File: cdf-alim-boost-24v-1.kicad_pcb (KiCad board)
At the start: 4 copper layers, 92 parts, among them J1 Conn_01x02, J2 Conn_01x02, J3 Conn_01x02, Q1 BSC019N04LS, Q2 BSC019N04LS, Q3 BSC019N04LS, Q4 BSC019N04LS, Q5 BSC019N04LS, U1 HT753-1, U2 TPS25983, U4 LM5122

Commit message: pcb: add +3V3 ldo layout
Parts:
- moved C1 7.19 mm to (191.5, 91.8), turned to 180 degrees
- moved TP4 6.05 mm to (196.5, 88.2), turned to 90 degrees
- moved C4 2.66 mm to (195.0, 91.8)
- moved U1 1.57 mm to (192.2, 87.8), turned to 90 degrees
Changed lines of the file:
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@@
 	(footprint "Capacitor_SMD:C_0805_2012Metric"
 		(layer "F.Cu")
-		(at 197.45 87.71)
+		(at 191.5 91.75 180)
 		(descr "Capacitor SMD 0805 (2012 Metric), square (rectangular) end terminal, IPC-7351 nominal, (Body size source: IPC-SM-782 page 76, https://www.pcb-3d.com/wordpress/wp-content/uploads/ipc-sm-782a_amendment_1_and_2.pdf, https://docs.google.com/spreadsheets/d/1BsfQQcO9C6DZCsRaXUlFlo91Tg2WpOkGARC1WS5S8t0/edit?usp=sharing)")
 		(tags "capacitor")
@@
 		)
 		(property "Basic" "Y"
-			(at 0 0 0)
+			(at 0 0 180)
 			(unlocked yes)
 			(layer "F.Fab")
@@
 		)
 		(property "JLCPCB Part #" "C440198"
-			(at 0 0 0)
+			(at 0 0 180)
 			(unlocked yes)
 			(layer "F.Fab")
@@
 		)
 		(property "Manufacturer" "Murata"
-			(at 0 0 0)
+			(at 0 0 180)
 			(unlocked yes)
 			(layer "F.Fab")
@@
 		)
 		(property "Manufacturer Part Number" "GRM21BR61H106KE43L"
-			(at 0 0 0)
+			(at 0 0 180)
 			(unlocked yes)
 			(layer "F.Fab")
@@
 		(duplicate_pad_numbers_are_jumpers no)
 		(fp_line
-			(start -0.261252 -0.735)
-			(end 0.261252 -0.735)
+			(start -0.261252 0.735)
+			(end 0.261252 0.735)
 			(stroke
 				(width 0.12)
@@
 		)
 		(fp_line
-			(start -0.261252 0.735)
-			(end 0.261252 0.735)
+			(start -0.261252 -0.735)
+			(end 0.261252 -0.735)
 			(stroke
 				(width 0.12)
@@
 		)
 		(pad "1" smd roundrect
-			(at -0.95 0)
+			(at -0.95 0 180)
 			(size 1 1.45)
 			(layers "F.Cu" "F.Mask" "F.Paste")
@@
 		)
 		(pad "2" smd roundrect
-			(at 0.95 0)
+			(at 0.95 0 180)
 			(size 1 1.45)
 			(layers "F.Cu" "F.Mask" "F.Paste")
@@
 	(footprint "TestPoint:TestPoint_Pad_D2.0mm"
 		(layer "F.Cu")
-		(at 197.25 94.25)
+		(at 196.5 88.25 90)
 		(descr "SMD pad as test Point, diameter 2.0mm")
 		(tags "test point SMD pad")
 		(property "Reference" "TP4"
-			(at 0 -1.998 0)
+			(at 0 -1.998 90)
 			(layer "F.SilkS")
 			(effects
@@
 		)
 		(property "Value" "TestPoint"
-			(at 0 2.05 0)
+			(at 0 2.05 90)
 			(layer "F.Fab")
 			(effects
@@
 		)
 		(property "Datasheet" ""
-			(at 0 0 0)
+			(at 0 0 90)
 			(unlocked yes)
 			(layer "F.Fab")
@@
 		)
 		(property "Description" "test point"
-			(at 0 0 0)
+			(at 0 0 90)
 			(unlocked yes)
 			(layer "F.Fab")
@@
 		)
 		(fp_text user "${REFERENCE}"
-			(at 0 -2 0)
+			(at 0 -2 90)
 			(layer "F.Fab")
 			(effects
@@
 		)
 		(pad "1" smd circle
-			(at 0 0)
+			(at 0 0 90)
 			(size 2 2)
 			(layers "F.Cu" "F.Mask")
@@
 	(footprint "Package_TO_SOT_SMD:SOT-89-3"
 		(layer "F.Cu")
-		(at 192.45 89.305)
+		(at 192.25 87.75 90)
 		(descr "SOT-89-3, http://ww1.microchip.com/downloads/en/DeviceDoc/3L_SOT-89_MB_C04-029C.pdf")
 		(tags "SOT-89-3")
 		(property "Reference" "U1"
-			(at 0 -3.5 0)
+			(at 0 -3.5 90)
 			(layer "F.SilkS")
 			(effects
@@
 		)
 		(property "Value" "HT753-1"
-			(at 0 3.5 0)
+			(at 0 3.5 90)
 			(layer "F.Fab")
 			(effects
@@
 		)
 		(property "Datasheet" "https://www.holtek.com/documents/10179/116711/HT75xx-1v250.pdf"
-			(at 0 0 0)
+			(at 0 0 90)
 			(unlocked yes)
 			(layer "F.Fab")
@@
 		)
 		(property "Description" "100mA Low Dropout Voltage Regulator, Fixed Output, SOT89"
-			(at 0 0 0)
+			(at 0 0 90)
 			(unlocked yes)
 			(layer "F.Fab")
@@
 		)
 		(property "Basic" "Y"
-			(at 0 0 0)
+			(at 0 0 90)
 			(unlocked yes)
 			(layer "F.Fab")
@@
 		)
 		(property "JLCPCB Part #" "C14289"
-			(at 0 0 0)
+			(at 0 0 90)
 			(unlocked yes)
 			(layer "F.Fab")
@@
 		)
 		(property "Manufacturer" "Holtek Semicon"
-			(at 0 0 0)
+			(at 0 0 90)
 			(unlocked yes)
 			(layer "F.Fab")
@@
 		)
 		(property "Manufacturer Part Number" "HT7533-1"
-			(at 0 0 0)
+			(at 0 0 90)
 			(unlocked yes)
 			(layer "F.Fab")
@@
 		)
 		(fp_line
-			(start -2.85 2.5)
+			(start 2.25 -2.5)
 			(end -2.85 -2.5)
 			(stroke
@@
 		)
 		(fp_line
-			(start -2.85 2.5)
+			(start 2.25 -2.5)
 			(end 2.25 2.5)
 			(stroke
@@
 		)
 		(fp_line
-			(start 2.25 -2.5)
+			(start -2.85 2.5)
 			(end -2.85 -2.5)
 			(stroke
@@
 		)
 		(fp_line
-			(start 2.25 -2.5)
+			(start -2.85 2.5)
 			(end 2.25 2.5)
 			(stroke
@@
 		)
 		(fp_line
-			(start -1.25 -1.25)
-			(end -0.25 -2.25)
+			(start 1.25 -2.25)
+			(end 1.25 2.25)
 			(stroke
 				(width 0.1)
@@
 		)
 		(fp_line
-			(start -1.25 2.25)
-			(end -1.25 -1.25)
+			(start -0.25 -2.25)
+			(end 1.25 -2.25)
 			(stroke
 				(width 0.1)
@@
 		)
 		(fp_line
-			(start -0.25 -2.25)
-			(end 1.25 -2.25)
+			(start -1.25 -1.25)
+			(end -0.25 -2.25)
 			(stroke
 				(width 0.1)
@@
 		)
 		(fp_line
-			(start 1.25 -2.25)
-			(end 1.25 2.25)
+			(start 1.25 2.25)
+			(end -1.25 2.25)
 			(stroke
 				(width 0.1)
@@
 		)
 		(fp_line
-			(start 1.25 2.25)
-			(end -1.25 2.25)
+			(start -1.25 2.25)
+			(end -1.25 -1.25)
 			(stroke
 				(width 0.1)
@@
 		)
 		(fp_text user "${REFERENCE}"
-			(at 0.2 0 90)
+			(at 0.2 0 0)
 			(layer "F.Fab")
 			(effects
@@
 		)
 		(pad "1" smd roundrect
-			(at -1.95 -1.5)
+			(at -1.95 -1.5 90)
 			(size 1.3 0.9)
 			(layers "F.Cu" "F.Mask" "F.Paste")
@@
 		)
 		(pad "2" smd custom
-			(at -1.8625 0)
+			(at -1.8625 0 90)
 			(size 1.475 0.9)
 			(layers "F.Cu" "F.Mask" "F.Paste")
@@
 		)
 		(pad "3" smd roundrect
-			(at -1.95 1.5)
+			(at -1.95 1.5 90)
 			(size 1.3 0.9)
 			(layers "F.Cu" "F.Mask" "F.Paste")
@@
 	(footprint "Capacitor_SMD:C_0805_2012Metric"
 		(layer "F.Cu")
-		(at 197.45 90.72)
+		(at 195 91.75)
 		(descr "Capacitor SMD 0805 (2012 Metric), square (rectangular) end terminal, IPC-7351 nominal, (Body size source: IPC-SM-782 page 76, https://www.pcb-3d.com/wordpress/wp-content/uploads/ipc-sm-782a_amendment_1_and_2.pdf, https://docs.google.com/spreadsheets/d/1BsfQQcO9C6DZCsRaXUlFlo91Tg2WpOkGARC1WS5S8t0/edit?usp=sharing)")
 		(tags "capacitor")

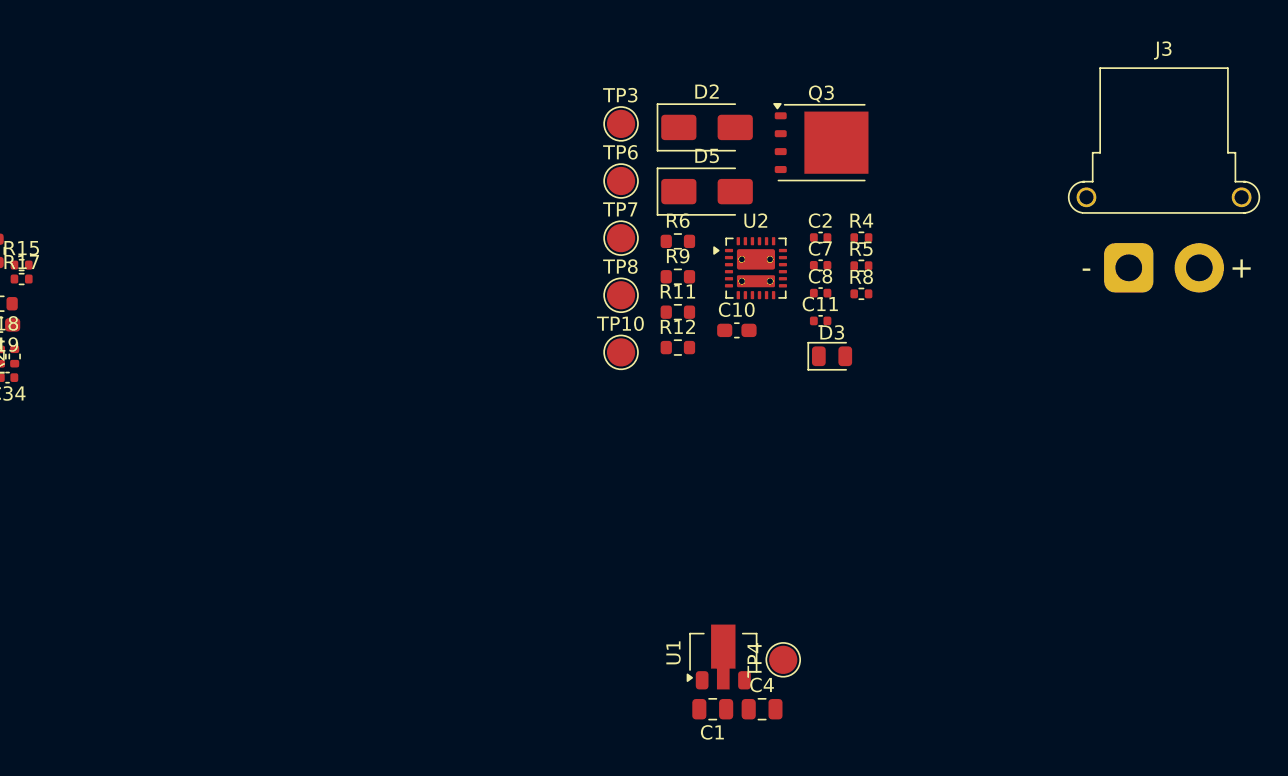
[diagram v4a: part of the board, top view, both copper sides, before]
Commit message: pcb: add efuse layout
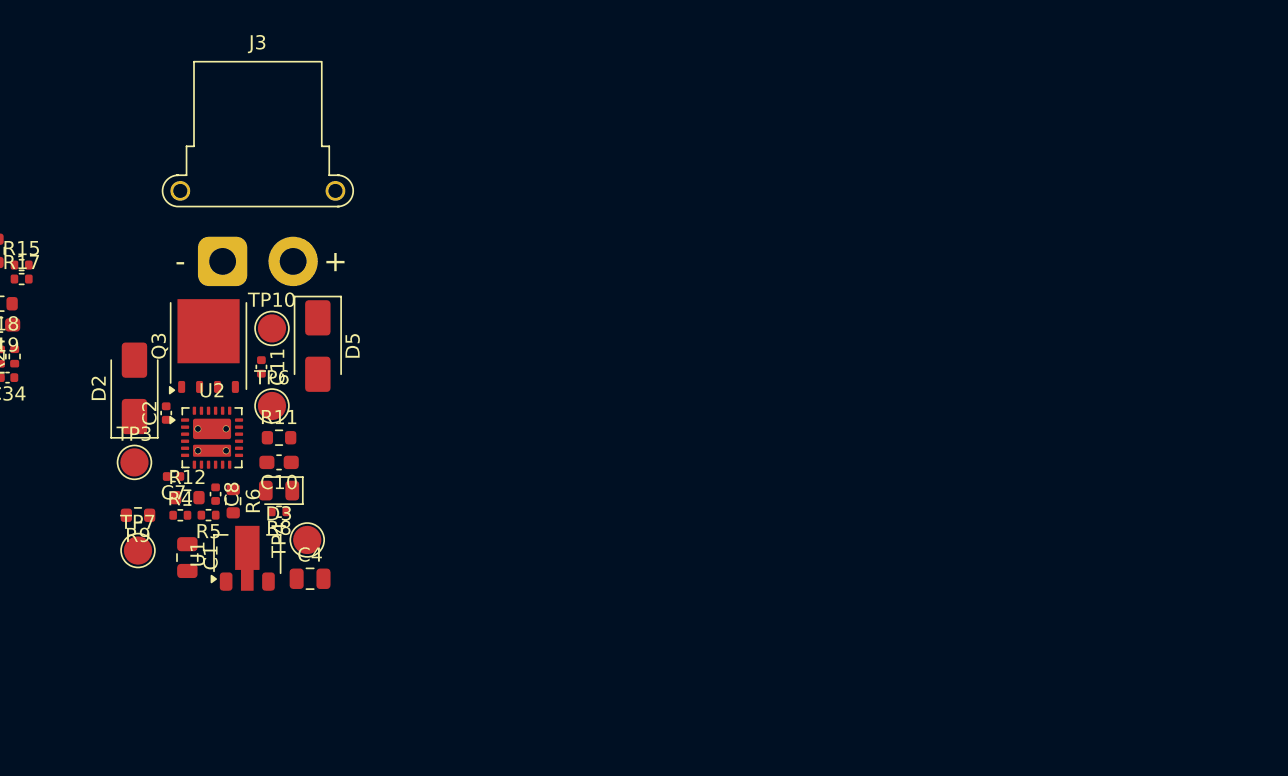
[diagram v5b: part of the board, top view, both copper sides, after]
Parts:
- removed TP8: TestPoint, TestPoint:TestPoint_Pad_D2.0mm
- moved J3 64.3 mm to (156.8, 60.0)
- moved R4 52.1 mm to (153.8, 78.0)
- moved R5 49.6 mm to (155.8, 78.0), turned to 180 degrees
- moved C7 48.3 mm to (153.3, 75.2), turned to 180 degrees
- moved C2 48.0 mm to (152.8, 70.8), turned to 90 degrees
- moved Q3 45.8 mm to (155.8, 66.0), turned to 90 degrees
- moved C8 45.2 mm to (156.2, 76.5), turned to -90 degrees
- moved D2 44.6 mm to (150.5, 69.0), turned to 90 degrees
- moved R8 44.1 mm to (160.8, 77.8), turned to 180 degrees
- moved TP3 42.0 mm to (150.5, 74.2)
- moved R9 41.8 mm to (150.8, 78.0), turned to 180 degrees
- moved TP7 40.8 mm to (150.8, 80.5)
- moved U2 40.4 mm to (156.0, 72.5)
- moved D3 40.4 mm to (160.8, 76.2), turned to 180 degrees
- moved C11 39.8 mm to (159.5, 67.5), turned to -90 degrees
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
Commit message: pcb: initial placement
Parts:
- removed TP11: TestPoint, TestPoint:TestPoint_Pad_D2.0mm
- added FID1: Fiducial, Fiducial:Fiducial_1mm_Mask2mm, F.Cu at (72.0, 81.0)
- added FID2: Fiducial, Fiducial:Fiducial_1mm_Mask2mm, F.Cu at (49.0, 58.0)
- added FID3: Fiducial, Fiducial:Fiducial_1mm_Mask2mm, F.Cu at (112.0, 61.0)
- added H1: MountingHole, MountingHole:ToolingHole_1.152mm, F.Cu at (60.0, 78.0)
- added H2: MountingHole, MountingHole:ToolingHole_1.152mm, F.Cu at (100.0, 83.0)
- added H3: MountingHole, MountingHole:ToolingHole_1.152mm, F.Cu at (78.0, 43.0)
- added H4: MountingHole_Pad, MountingHole:MountingHole_3.2mm_M3_Pad_Via, F.Cu at (66.0, 81.0)
- added H5: MountingHole_Pad, MountingHole:MountingHole_3.2mm_M3_Pad_Via, F.Cu at (88.0, 45.0)
- added H6: MountingHole_Pad, MountingHole:MountingHole_3.2mm_M3_Pad_Via, F.Cu at (111.0, 67.0)
- moved D5 99.4 mm to (66.0, 46.8), turned to 0 degrees
- moved J3 97.0 mm to (60.0, 53.5), turned to 90 degrees
- moved TP10 96.6 mm to (64.8, 50.0), turned to 90 degrees
- moved C11 93.5 mm to (67.5, 50.8), turned to 0 degrees
- moved TP6 92.2 mm to (70.2, 50.0), turned to 90 degrees
- moved R11 91.2 mm to (72.5, 49.5), turned to 90 degrees
- moved Q3 90.5 mm to (66.0, 54.5), turned to 180 degrees
- moved C10 90.0 mm to (74.2, 49.5), turned to -90 degrees
- moved TP4 89.0 mm to (79.8, 47.5), turned to 180 degrees
- moved D3 88.6 mm to (76.2, 49.5), turned to -90 degrees
- moved C4 87.8 mm to (82.5, 47.3), turned to 90 degrees
- moved R8 87.7 mm to (77.8, 49.5), turned to -90 degrees
- moved U2 85.5 mm to (72.5, 54.2), turned to 90 degrees
- moved R9 84.4 mm to (72.5, 46.2), turned to -90 degrees
- moved R6 84.1 mm to (77.0, 52.8), turned to 0 degrees
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
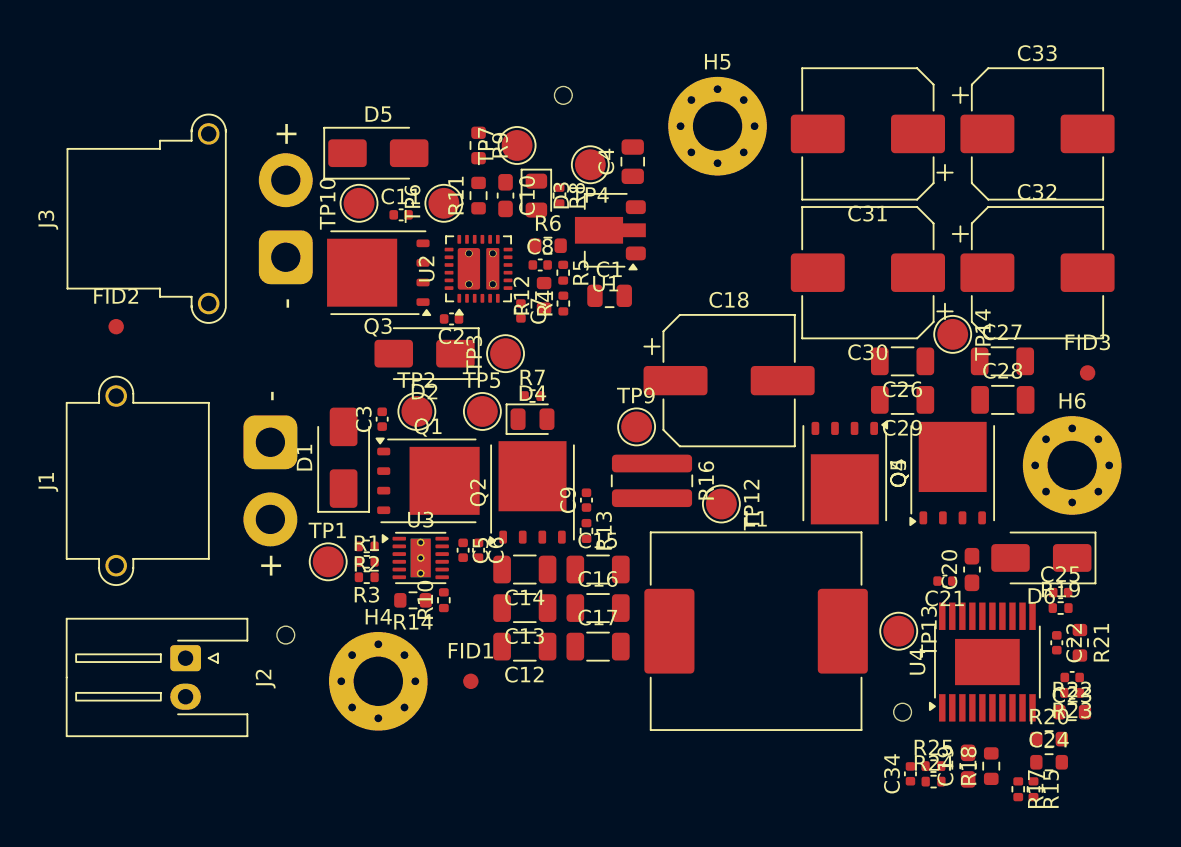
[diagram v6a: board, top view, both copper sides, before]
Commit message: pcb: add board outline
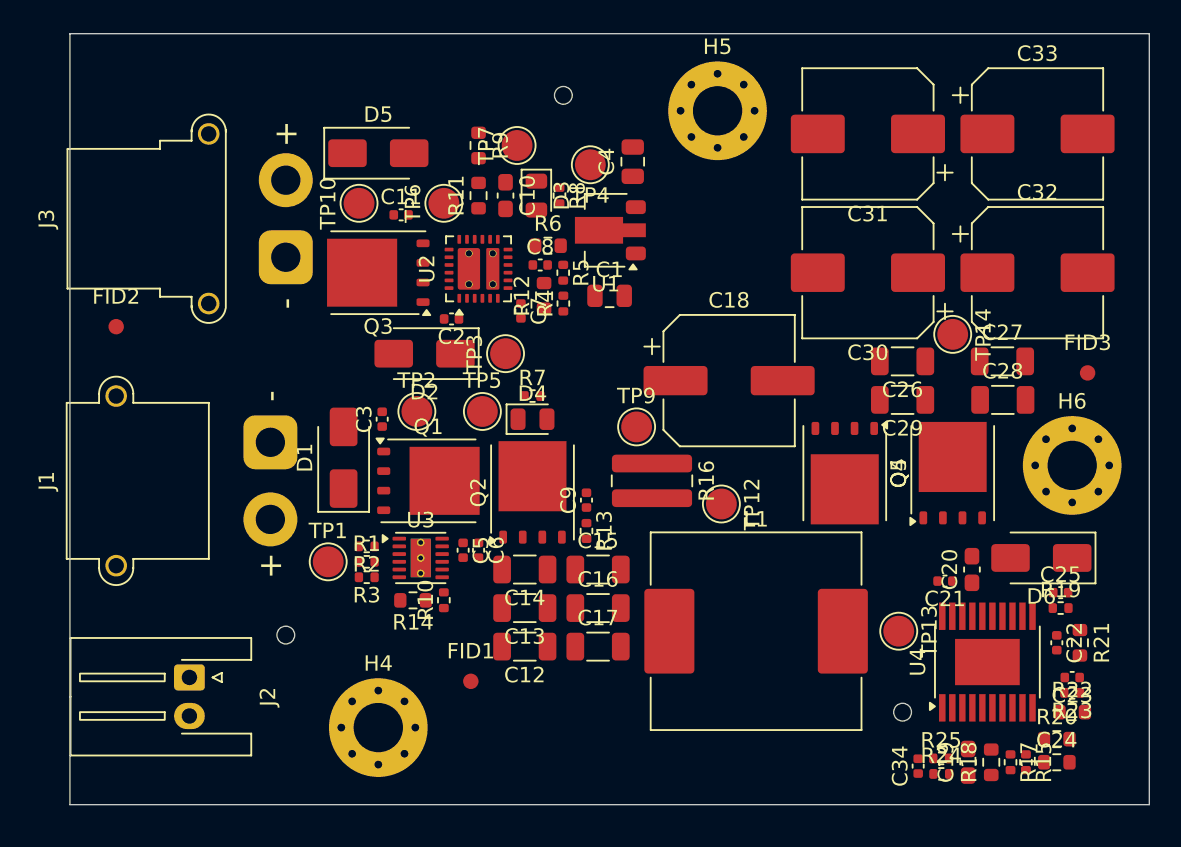
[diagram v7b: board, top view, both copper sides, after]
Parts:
- moved H4 3.00 mm to (66.0, 84.0)
- moved R17 1.82 mm to (107.0, 86.2)
- moved R15 1.82 mm to (108.0, 86.2)
- moved J2 1.27 mm to (53.8, 80.8)
- moved H5 1.00 mm to (88.0, 44.0)
- moved C34 0.71 mm to (101.0, 86.5)
- moved R24 0.71 mm to (102.5, 87.0)
- moved R25 0.71 mm to (102.5, 86.0)
- moved C24 0.50 mm to (110.0, 86.2)
- moved R20 0.50 mm to (110.0, 84.8)
- moved C19 0.25 mm to (104.2, 86.2)
- moved R18 0.25 mm to (105.8, 86.2)
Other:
- board outline added: 70 x 50 mm
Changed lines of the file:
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@@
 	(footprint "Resistor_SMD:R_0402_1005Metric"
 		(layer "F.Cu")
-		(at 102 86.5)
+		(at 102.5 86)
 		(descr "Resistor SMD 0402 (1005 Metric), square (rectangular) end terminal, IPC-7351 nominal, (Body size source: IPC-SM-782 page 72, https://www.pcb-3d.com/wordpress/wp-content/uploads/ipc-sm-782a_amendment_1_and_2.pdf)")
 		(tags "resistor")
@@
 	(footprint "MountingHole:MountingHole_3.2mm_M3_Pad_Via"
 		(layer "F.Cu")
-		(at 88 45)
+		(at 88 44)
 		(descr "Mounting Hole 3.2mm, M3, generated by kicad-footprint-generator mountinghole.py")
 		(tags "mountinghole M3")
@@
 	(footprint "Capacitor_SMD:C_0603_1608Metric_Pad1.08x0.95mm_HandSolder"
 		(layer "F.Cu")
-		(at 104.25 86.5 90)
+		(at 104.25 86.25 90)
 		(descr "Capacitor SMD 0603 (1608 Metric), square (rectangular) end terminal, IPC-7351 nominal with elongated pad for handsoldering. (Body size source: IPC-SM-782 page 76, https://www.pcb-3d.com/wordpress/wp-content/uploads/ipc-sm-782a_amendment_1_and_2.pdf)")
 		(tags "capacitor handsolder")
@@
 	(footprint "Resistor_SMD:R_0402_1005Metric"
 		(layer "F.Cu")
-		(at 102.01 87.505)
+		(at 102.51 87.005)
 		(descr "Resistor SMD 0402 (1005 Metric), square (rectangular) end terminal, IPC-7351 nominal, (Body size source: IPC-SM-782 page 72, https://www.pcb-3d.com/wordpress/wp-content/uploads/ipc-sm-782a_amendment_1_and_2.pdf)")
 		(tags "resistor")
@@
 	(footprint "Resistor_SMD:R_0603_1608Metric"
 		(layer "F.Cu")
-		(at 109.5 86.25)
+		(at 110 86.25)
 		(descr "Resistor SMD 0603 (1608 Metric), square (rectangular) end terminal, IPC-7351 nominal, (Body size source: IPC-SM-782 page 72, https://www.pcb-3d.com/wordpress/wp-content/uploads/ipc-sm-782a_amendment_1_and_2.pdf)")
 		(tags "resistor")
@@
 	(footprint "Resistor_SMD:R_0402_1005Metric"
 		(layer "F.Cu")
-		(at 107.5 88 -90)
+		(at 107 86.25 -90)
 		(descr "Resistor SMD 0402 (1005 Metric), square (rectangular) end terminal, IPC-7351 nominal, (Body size source: IPC-SM-782 page 72, https://www.pcb-3d.com/wordpress/wp-content/uploads/ipc-sm-782a_amendment_1_and_2.pdf)")
 		(tags "resistor")
@@
 	(footprint "Resistor_SMD:R_0603_1608Metric"
 		(layer "F.Cu")
-		(at 109.5 84.75)
+		(at 110 84.75)
 		(descr "Resistor SMD 0603 (1608 Metric), square (rectangular) end terminal, IPC-7351 nominal, (Body size source: IPC-SM-782 page 72, https://www.pcb-3d.com/wordpress/wp-content/uploads/ipc-sm-782a_amendment_1_and_2.pdf)")
 		(tags "resistor")
@@
 	(footprint "Resistor_SMD:R_0603_1608Metric"
 		(layer "F.Cu")
-		(at 105.75 86.5 90)
+		(at 105.75 86.25 90)
 		(descr "Resistor SMD 0603 (1608 Metric), square (rectangular) end terminal, IPC-7351 nominal, (Body size source: IPC-SM-782 page 72, https://www.pcb-3d.com/wordpress/wp-content/uploads/ipc-sm-782a_amendment_1_and_2.pdf)")
 		(tags "resistor")
@@
 	(footprint "Resistor_SMD:R_0402_1005Metric"
 		(layer "F.Cu")
-		(at 108.49 88 -90)
+		(at 108 86.25 -90)
 		(descr "Resistor SMD 0402 (1005 Metric), square (rectangular) end terminal, IPC-7351 nominal, (Body size source: IPC-SM-782 page 72, https://www.pcb-3d.com/wordpress/wp-content/uploads/ipc-sm-782a_amendment_1_and_2.pdf)")
 		(tags "resistor")
@@
 	(footprint "Capacitor_SMD:C_0402_1005Metric"
 		(layer "F.Cu")
-		(at 100.51 87 90)
+		(at 101.01 86.5 90)
 		(descr "Capacitor SMD 0402 (1005 Metric), square (rectangular) end terminal, IPC-7351 nominal, (Body size source: IPC-SM-782 page 76, https://www.pcb-3d.com/wordpress/wp-content/uploads/ipc-sm-782a_amendment_1_and_2.pdf)")
 		(tags "capacitor")
@@
 	(footprint "Connector_JST:JST_XH_S2B-XH-A-1_1x02_P2.50mm_Horizontal"
 		(layer "F.Cu")
-		(at 53.5 79.5 -90)
+		(at 53.75 80.75 -90)
 		(descr "JST XH series connector, S2B-XH-A-1 (http://www.jst-mfg.com/product/pdf/eng/eXH.pdf)")
 		(tags "connector JST XH horizontal")
@@
 	(footprint "MountingHole:MountingHole_3.2mm_M3_Pad_Via"
 		(layer "F.Cu")
-		(at 66 81)
+		(at 66 84)
 		(descr "Mounting Hole 3.2mm, M3, generated by kicad-footprint-generator mountinghole.py")
 		(tags "mountinghole M3")
@@
 		(embedded_fonts no)
 	)
+	(gr_rect
+		(start 46 39)
+		(end 116 89)
+		(radius 3)
+		(stroke
+			(width 0.05)
+			(type solid)
+		)
+		(fill no)
+		(layer "Edge.Cuts")
+	)
 	(segment

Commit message: pcb: center board
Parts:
- moved C7 74.8 mm to (144.2, 86.0)
- moved R5 74.8 mm to (147.0, 83.5)
- moved C1 74.8 mm to (150.0, 85.0)
- moved C10 74.8 mm to (143.2, 78.5)
- moved C11 74.8 mm to (136.5, 79.8)
- moved C12 74.8 mm to (144.5, 107.8)
- moved C13 74.8 mm to (144.5, 105.2)
- moved C14 74.8 mm to (144.5, 102.8)
- moved C15 74.8 mm to (149.2, 102.8)
- moved C16 74.8 mm to (149.2, 105.2)
- moved C17 74.8 mm to (149.2, 107.8)
- moved C18 74.8 mm to (157.8, 90.5)
- moved C19 74.8 mm to (173.2, 115.2)
- moved C2 74.8 mm to (139.8, 86.5)
- moved C20 74.8 mm to (173.5, 102.8)
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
